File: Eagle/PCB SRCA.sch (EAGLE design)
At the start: 75 parts, among them IC1 DSPIC30F4011-30I_P, IC2 LM324LVIDR, IC3 LMT86QDCKRQ1, IC5 FT232RL-REEL, J1 TBL002A-350-03GR-2OR, J2 TBL002A-350-03GR-2OR, J3 TBL002A-350-03GR-2OR, J4 44914-0801, J6 TBL002A-350-03GR-2OR, J7 44914-0401, Q1 TIP41C, T1 2N3904, T12 2N3904, T13 2N3904, T2 2N3904, T3 2N3904, T4 2N3904, T5 2N3904, T6 2N3904, T7 2N3904

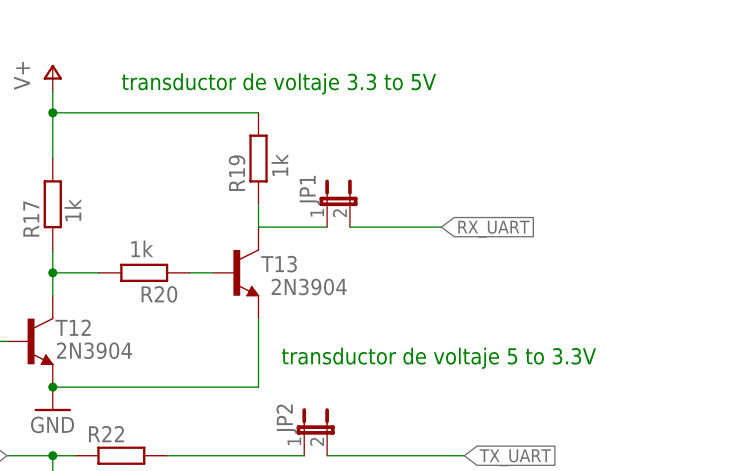
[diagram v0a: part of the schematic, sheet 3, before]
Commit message: 24-08-2021
correccion de errores en pistas
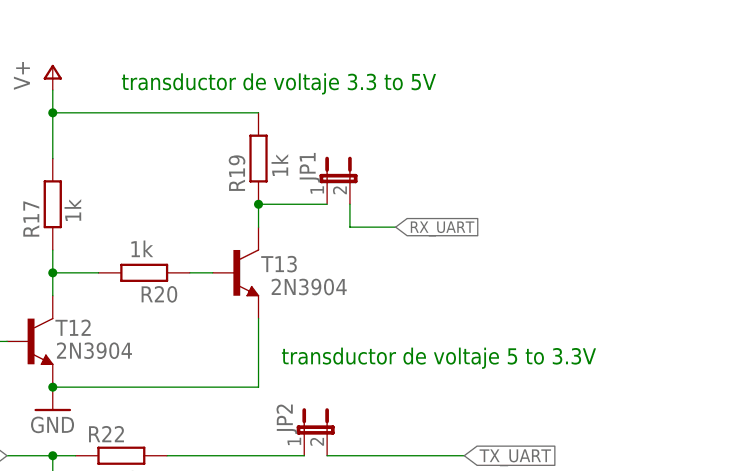
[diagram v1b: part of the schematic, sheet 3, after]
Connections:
- removed net N$14: IC5.RESET#, IC5.VCC, IC5.VCCIO
- net V+: now also IC5.RESET#, IC5.VCC, IC5.VCCIO
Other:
- note added: "2.7k"
- note added: "4.7k"
- note added: "6.8k"
- moved on the sheet: JP1
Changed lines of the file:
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@@
 <text x="153" y="134" size="1.778" layer="95">104</text>
 <text x="221" y="73" size="1.778" layer="95" rot="R90">1k</text>
+<text x="173" y="111" size="1.778" layer="96" rot="R90">4.7k</text>
+<text x="184" y="111" size="1.778" layer="96" rot="R90">4.7k</text>
+<text x="92" y="48" size="1.778" layer="96" rot="R90">6.8k</text>
+<text x="102" y="67" size="1.778" layer="96" rot="R180">2.7k</text>
 </plain>
 <instances>
@@
 <wire x1="208.28" y1="170.18" x2="200.66" y2="170.18" width="0.1524" layer="91"/>
 <pinref part="ICS" gate="G$1" pin="1"/>
-<wire x1="200.66" y1="152.4" x2="200.66" y2="162.56" width="0.1524" layer="91"/>
+<wire x1="200.66" y1="152.4" x2="200.66" y2="165.1" width="0.1524" layer="91"/>
 <pinref part="P+3" gate="1" pin="V+"/>
-<wire x1="200.66" y1="162.56" x2="200.66" y2="170.18" width="0.1524" layer="91"/>
+<wire x1="200.66" y1="165.1" x2="200.66" y2="170.18" width="0.1524" layer="91"/>
 <wire x1="208.28" y1="172.72" x2="208.28" y2="170.18" width="0.1524" layer="91"/>
 <junction x="208.28" y="170.18"/>
 <pinref part="R1" gate="G$1" pin="2"/>
-<wire x1="200.66" y1="162.56" x2="190.5" y2="162.56" width="0.1524" layer="91"/>
+<wire x1="190.5" y1="162.56" x2="190.5" y2="165.1" width="0.1524" layer="91"/>
+<wire x1="190.5" y1="165.1" x2="200.66" y2="165.1" width="0.1524" layer="91"/>
+<junction x="200.66" y="165.1"/>
 </segment>
 <segment>
@@
 </segment>
 <segment>
-<pinref part="P+20" gate="1" pin="V+"/>
-<wire x1="53" y1="69.46" x2="53" y2="66" width="0.1524" layer="91"/>
-</segment>
-<segment>
 <wire x1="13" y1="24" x2="20" y2="24" width="0.1524" layer="91"/>
 <pinref part="P+21" gate="1" pin="V+"/>
@@
 <pinref part="C6" gate="G$1" pin="+"/>
 </segment>
-</net>
-<net name="SONAR_ADC2" class="0">
-<segment>
-<pinref part="J6" gate="G$1" pin="A1"/>
-<wire x1="238.76" y1="53.34" x2="238.76" y2="43.18" width="0.1524" layer="91"/>
-<label x="238.76" y="43.18" size="1.4224" layer="95" rot="R180" xref="yes"/>
-</segment>
-</net>
-<net name="L_SONAR2_DATA" class="0">
-<segment>
-<wire x1="190.5" y1="111.76" x2="187.96" y2="111.76" width="0.1524" layer="91"/>
-<label x="187.96" y="111.76" size="1.778" layer="95" rot="R180" xref="yes"/>
-<pinref part="T6" gate="G1" pin="B"/>
-</segment>
-</net>
-<net name="L_RX_DATA" class="0">
-<segment>
-<wire x1="226.06" y1="111.76" x2="223.52" y2="111.76" width="0.1524" layer="91"/>
-<label x="223.52" y="111.76" size="1.778" layer="95" rot="R180" xref="yes"/>
-<pinref part="T7" gate="G1" pin="B"/>
-</segment>
-</net>
-<net name="N$15" class="0">
-<segment>
-<pinref part="IC5" gate="G$1" pin="CBUS0"/>
-<wire x1="71.12" y1="43.18" x2="86.36" y2="43.18" width="0.1524" layer="91"/>
-<pinref part="LED7" gate="G$1" pin="K"/>
-<wire x1="86.36" y1="48.26" x2="86.36" y2="43.18" width="0.1524" layer="91"/>
-</segment>
-</net>
-<net name="N$18" class="0">
-<segment>
-<pinref part="IC5" gate="G$1" pin="CBUS1"/>
-<wire x1="71.12" y1="40.64" x2="96.52" y2="40.64" width="0.1524" layer="91"/>
-<pinref part="LED8" gate="G$1" pin="K"/>
-<wire x1="96.52" y1="40.64" x2="96.52" y2="48.26" width="0.1524" layer="91"/>
-</segment>
-</net>
-<net name="N$3" class="0">
-<segment>
-<pinref part="LED7" gate="G$1" pin="A"/>
-<pinref part="R12" gate="G$1" pin="1"/>
-<wire x1="86.36" y1="63.5" x2="86.36" y2="68.58" width="0.1524" layer="91"/>
-</segment>
-</net>
-<net name="N$13" class="0">
-<segment>
-<pinref part="R13" gate="G$1" pin="1"/>
-<pinref part="LED8" gate="G$1" pin="A"/>
-<wire x1="96.52" y1="68.58" x2="96.52" y2="63.5" width="0.1524" layer="91"/>
-</segment>
-</net>
-<net name="N$14" class="0">
 <segment>
 <pinref part="IC5" gate="G$1" pin="VCCIO"/>
 <wire x1="38.1" y1="48.26" x2="30.48" y2="48.26" width="0.1524" layer="91"/>
 <wire x1="30.48" y1="48.26" x2="30.48" y2="66.04" width="0.1524" layer="91"/>
-<wire x1="30.48" y1="66.04" x2="73.66" y2="66.04" width="0.1524" layer="91"/>
+<wire x1="30.48" y1="66.04" x2="53" y2="66.04" width="0.1524" layer="91"/>
+<wire x1="53.34" y1="66.04" x2="73.66" y2="66.04" width="0.1524" layer="91"/>
 <wire x1="73.66" y1="66.04" x2="73.66" y2="35.56" width="0.1524" layer="91"/>
 <pinref part="IC5" gate="G$1" pin="VCC"/>
@@
 <wire x1="73.66" y1="33.02" x2="73.66" y2="35.56" width="0.1524" layer="91"/>
 <junction x="73.66" y="35.56"/>
+<pinref part="P+20" gate="1" pin="V+"/>
+<wire x1="53.34" y1="66.04" x2="53" y2="66.04" width="0.1524" layer="91"/>
+<wire x1="53" y1="66.04" x2="53" y2="69.46" width="0.1524" layer="91"/>
+</segment>
+</net>
+<net name="SONAR_ADC2" class="0">
+<segment>
+<pinref part="J6" gate="G$1" pin="A1"/>
+<wire x1="238.76" y1="53.34" x2="238.76" y2="43.18" width="0.1524" layer="91"/>
+<label x="238.76" y="43.18" size="1.4224" layer="95" rot="R180" xref="yes"/>
+</segment>
+</net>
+<net name="L_SONAR2_DATA" class="0">
+<segment>
+<wire x1="190.5" y1="111.76" x2="187.96" y2="111.76" width="0.1524" layer="91"/>
+<label x="187.96" y="111.76" size="1.778" layer="95" rot="R180" xref="yes"/>
+<pinref part="T6" gate="G1" pin="B"/>
+</segment>
+</net>
+<net name="L_RX_DATA" class="0">
+<segment>
+<wire x1="226.06" y1="111.76" x2="223.52" y2="111.76" width="0.1524" layer="91"/>
+<label x="223.52" y="111.76" size="1.778" layer="95" rot="R180" xref="yes"/>
+<pinref part="T7" gate="G1" pin="B"/>
+</segment>
+</net>
+<net name="N$15" class="0">
+<segment>
+<pinref part="IC5" gate="G$1" pin="CBUS0"/>
+<wire x1="71.12" y1="43.18" x2="86.36" y2="43.18" width="0.1524" layer="91"/>
+<pinref part="LED7" gate="G$1" pin="K"/>
+<wire x1="86.36" y1="48.26" x2="86.36" y2="43.18" width="0.1524" layer="91"/>
+</segment>
+</net>
+<net name="N$18" class="0">
+<segment>
+<pinref part="IC5" gate="G$1" pin="CBUS1"/>
+<wire x1="71.12" y1="40.64" x2="96.52" y2="40.64" width="0.1524" layer="91"/>
+<pinref part="LED8" gate="G$1" pin="K"/>
+<wire x1="96.52" y1="40.64" x2="96.52" y2="48.26" width="0.1524" layer="91"/>
+</segment>
+</net>
+<net name="N$3" class="0">
+<segment>
+<pinref part="LED7" gate="G$1" pin="A"/>
+<pinref part="R12" gate="G$1" pin="1"/>
+<wire x1="86.36" y1="63.5" x2="86.36" y2="68.58" width="0.1524" layer="91"/>
+</segment>
+</net>
+<net name="N$13" class="0">
+<segment>
+<pinref part="R13" gate="G$1" pin="1"/>
+<pinref part="LED8" gate="G$1" pin="A"/>
+<wire x1="96.52" y1="68.58" x2="96.52" y2="63.5" width="0.1524" layer="91"/>
 </segment>
 </net>
@@
 <attribute name="VALUE" x="150.495" y="139.7" size="1.778" layer="96" rot="R90"/>
 </instance>
-<instance part="JP1" gate="A" x="147.32" y="165.1" smashed="yes">
-<attribute name="NAME" x="146.05" y="165.1" size="1.778" layer="95" rot="R90"/>
-<attribute name="VALUE" x="153.035" y="165.1" size="1.778" layer="96" rot="R90"/>
+<instance part="JP1" gate="A" x="147.32" y="167.64" smashed="yes">
+<attribute name="NAME" x="146.05" y="167.64" size="1.778" layer="95" rot="R90"/>
+<attribute name="VALUE" x="153.035" y="167.64" size="1.778" layer="96" rot="R90"/>
 </instance>
 <instance part="ICS1" gate="G$1" x="38.1" y="134.62" smashed="yes">
@@
 </segment>
 </net>
-<net name="RX_UART" class="0">
-<segment>
-<label x="160.02" y="162.56" size="1.4224" layer="95" xref="yes"/>
-<wire x1="149.86" y1="162.56" x2="160.02" y2="162.56" width="0.1524" layer="91"/>
-<pinref part="JP1" gate="A" pin="2"/>
-</segment>
-</net>
 <net name="TX_UART" class="0">
 <segment>
@@
 <net name="N$30" class="0">
 <segment>
+<pinref part="R19" gate="G$1" pin="1"/>
+<pinref part="JP1" gate="A" pin="1"/>
+<wire x1="139.7" y1="165.1" x2="147.32" y2="165.1" width="0.1524" layer="91"/>
 <pinref part="T13" gate="G1" pin="C"/>
-<pinref part="R19" gate="G$1" pin="1"/>
-<wire x1="139.7" y1="165.1" x2="139.7" y2="162.56" width="0.1524" layer="91"/>
-<wire x1="139.7" y1="162.56" x2="147.32" y2="162.56" width="0.1524" layer="91"/>
-<pinref part="JP1" gate="A" pin="1"/>
-</segment>
-</net>
+<wire x1="139.7" y1="162.56" x2="139.7" y2="165.1" width="0.1524" layer="91"/>
+<junction x="139.7" y="165.1"/>
+</segment>
+</net>
+<net name="RX_UART" class="0">
+<segment>
+<pinref part="JP1" gate="A" pin="2"/>
+<wire x1="149.86" y1="165.1" x2="149.86" y2="162.56" width="0.1524" layer="91"/>
+<wire x1="149.86" y1="162.56" x2="154.94" y2="162.56" width="0.1524" layer="91"/>
+<label x="154.94" y="162.56" size="1.27" layer="95" xref="yes"/>
+</segment>
+</net>

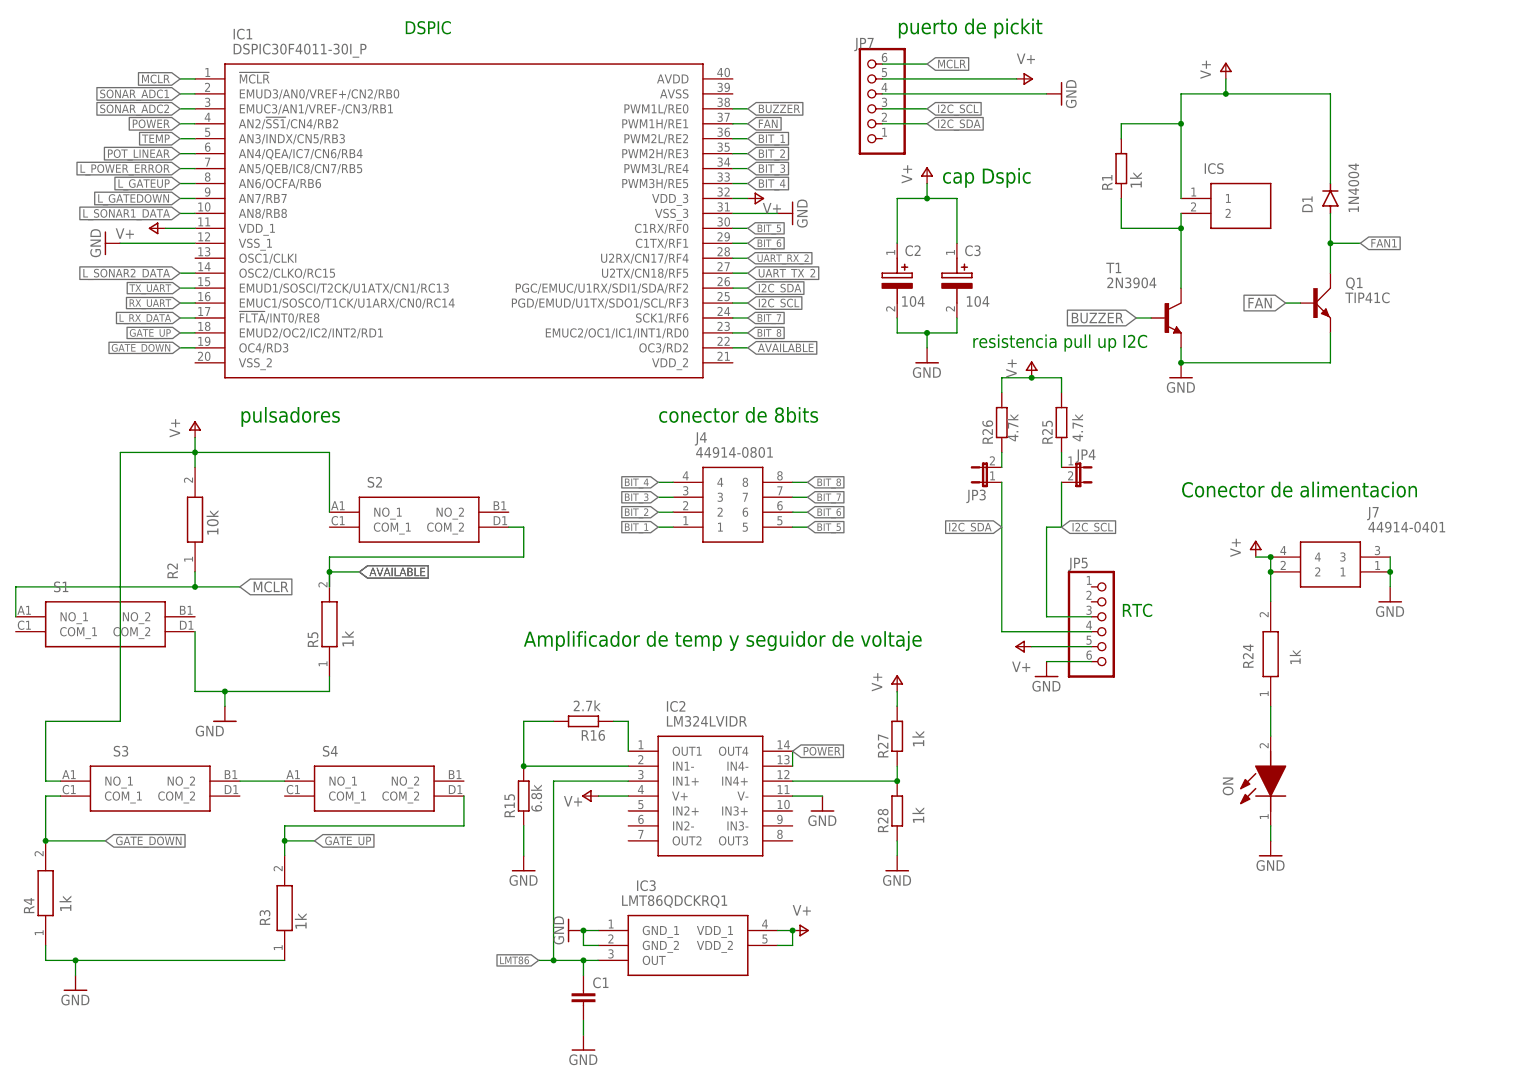
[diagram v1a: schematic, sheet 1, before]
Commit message: 26-08-2021
Actulizacion de la pcb correccion de pistas separacion entre ellas
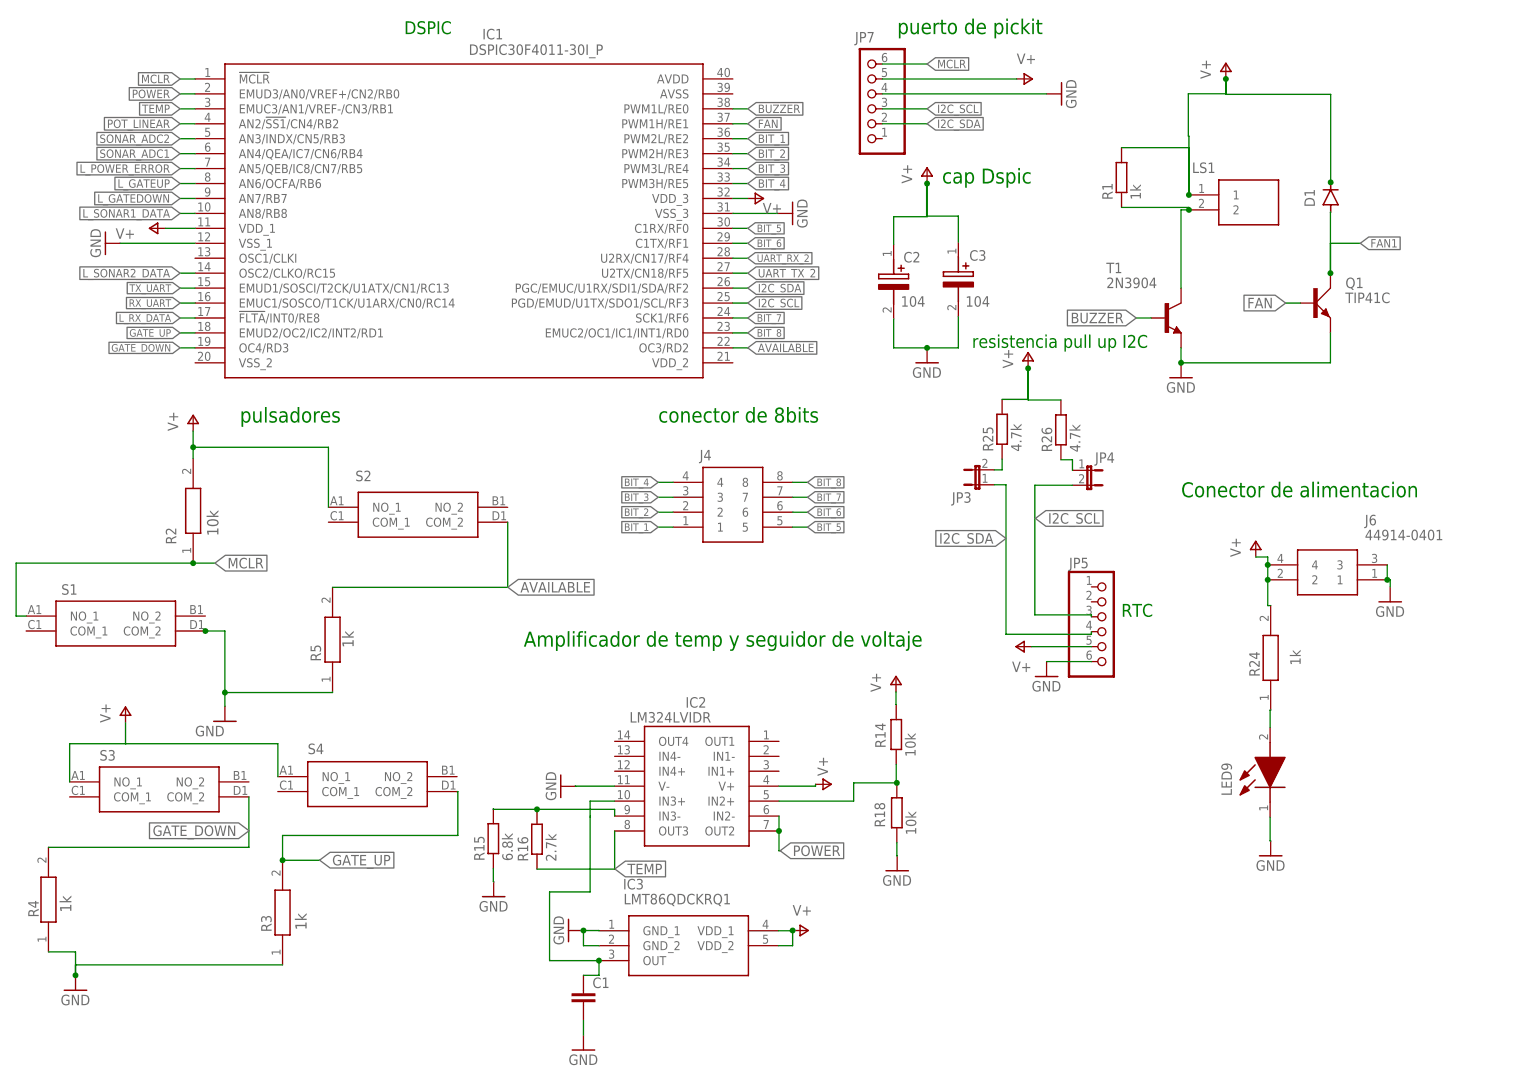
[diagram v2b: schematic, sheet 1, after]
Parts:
- removed IC5: FT232RL-REEL, FT232RL-REEL:FT232RL-REEL
- removed ICS: PS1240P02BT, PS1240P02BT:PS1240P02BT
- removed J7: 44914-0401, 44914-0401:44914-0401
- removed ON: 599-0181-007F, 599-0181-007F:599-0181-007F
- removed R27, R28: (no value), rcl:R-EU_0207/10
- added IC4: FT232RL-REEL, FT232RL-REEL:FT232RL-REEL
- added J5: TBL002A-350-03GR-2OR, TBL002A-350-03GR-2OR:TBL002A-350-03GR-2OR
- added LED9: 599-0181-007F, 599-0181-007F:599-0181-007F
- added LS1: PS1240P02BT, PS1240P02BT:PS1240P02BT
- added R14, R18: 10k, rcl:R-EU_0207/10
- D1: value 1N4004 -> 1N4148DO35-7; device diode:1N4004 -> diode:1N4148DO35-7
- J6: value TBL002A-350-03GR-2OR -> 44914-0401; device TBL002A-350-03GR-2OR:TBL002A-350-03GR-2OR -> 44914-0401:44914-0401
- R1: value (none) -> 1k; device rcl:R-EU_0204/7 -> rcl:R-EU_0207/10
- R15: value (none) -> 6.8k; device rcl:R-EU_0204/7 -> rcl:R-EU_0207/10
- R16: value (none) -> 2.7k; device rcl:R-EU_0204/7 -> rcl:R-EU_0207/10
- R17, R19, R20, R21: value (none) -> 1k
- R2: value ERA-6VEB1002V -> RC0805FR-071KL; device ERA-6VEB1002V:ERA-6VEB1002V -> RC0805FR-071KL:RC0805FR-071KL
- R22: value (none) -> 5.1k
- R23: value (none) -> 10k
- R25, R26: value (none) -> 4.7k; device rcl:R-EU_0204/7 -> rcl:R-EU_0207/10
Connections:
- removed net LMT86: C1.1, IC2.IN1+, IC3.OUT
- removed net N$15 (its old number): IC5.CBUS0, LED7.K
- removed net RESISTENCIA: IC2.IN1-, R15.2, R16.2
- removed net TEMP1: JP4.1, R25.1
- removed net TEMP2: JP3.2, R26.1
- removed net TEMP3: ICS.2, R1.1, T1.C
- new net N$19: JP3.2, R25.1
- new net N$25: LS1.2, R1.1, T1.C
- new net N$3: IC4.CBUS0, LED7.K
- new net N$31: JP4.1, R26.1
- new net N$32: IC2.IN2+, R14.1, R18.2
- net GATE_DOWN: now also S3.COM_2; no longer S3.COM_1
- net GND: now also C5.1, IC4.AGND, IC4.GND_1, IC4.GND_2, IC4.GND_3, IC4.TEST, J5.A2, J6.1, J6.3, LED9.K, R18.1; no longer C5.2, IC5.AGND, IC5.GND_1, IC5.GND_2, IC5.GND_3, IC5.TEST, J6.A2, J7.1, J7.3, ON.K, R28.1
- net N$1: now also IC2.IN3-, R15.2, R16.2; no longer S3.NO_2, S4.NO_1
- net N$18: now also IC4.CBUS1; no longer IC5.CBUS1
- net N$20: now also IC4.3V3OUT; no longer IC5.3V3OUT
- net N$21: now also IC4.USBDM; no longer IC5.USBDM
- net N$22: now also IC4.USBDP; no longer IC5.USBDP
- net N$27: now also C1.1, IC2.IN3+, IC3.OUT; no longer IC2.IN4+, R27.1, R28.2
- net N$28: now also LED9.A; no longer ON.A
- net POT_LINEAR: now also IC1.AN2/!SS1!/CN4/RB2; no longer IC1.AN4/QEA/IC7/CN6/RB4
- net POWER: now also IC1.EMUD3/AN0/VREF+/CN2/RB0, IC2.IN2-, IC2.OUT2; no longer IC1.AN2/!SS1!/CN4/RB2, IC2.IN4-, IC2.OUT4
- net SONAR_ADC1: now also IC1.AN4/QEA/IC7/CN6/RB4; no longer IC1.EMUD3/AN0/VREF+/CN2/RB0
- net SONAR_ADC2: now also IC1.AN3/INDX/CN5/RB3, J5.A1; no longer IC1.EMUC3/AN1/VREF-/CN3/RB1, J6.A1
- net TEMP: now also IC1.EMUC3/AN1/VREF-/CN3/RB1, IC2.OUT3; no longer IC1.AN3/INDX/CN5/RB3, IC2.OUT1
- net UART_RX_2: now also IC4.TXD; no longer IC5.TXD
- net UART_TX_2: now also IC4.RXD; no longer IC5.RXD
- net V+: now also C5.2, IC4.RESET#, IC4.VCC, IC4.VCCIO, J5.B1, J6.2, J6.4, LS1.1, R14.2, S4.NO_1; no longer C5.1, IC5.RESET#, IC5.VCC, IC5.VCCIO, ICS.1, J6.B1, J7.2, J7.4, R27.2
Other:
- note removed: "2.7k"
- note removed: "4.7k"
- note removed: "5.1k"
- note removed: "6.8k"
- moved on the sheet: C2, C4, C5, C6, IC2, JP2, JP3, JP4, LED3, LED5, LED6, LED8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
